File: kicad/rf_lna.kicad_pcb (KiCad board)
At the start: 4 copper layers, 100 x 100 mm, 69 parts, among them J1 Conn_01x02_Pin, J2 Conn_Coaxial_Small, J3 Conn_Coaxial_Small, J4 Conn_01x02_Pin, J5 Conn_Coaxial_Small, J6 Conn_Coaxial_Small, J7 Conn_Coaxial_Small, J8 Conn_Coaxial_Small, J9 Conn_Coaxial_Small, U1 L78L05_SOT89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

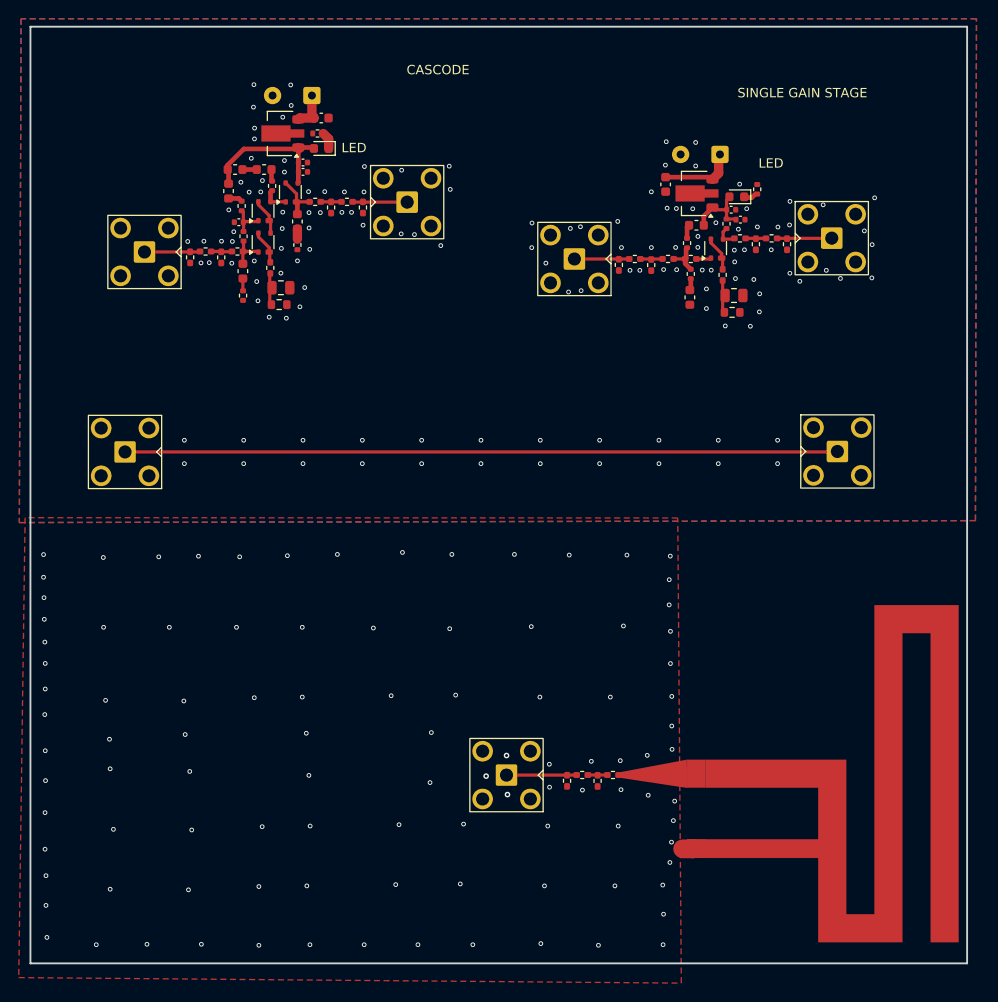
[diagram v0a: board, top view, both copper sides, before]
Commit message: files ready for production, but with wrong stackup (3313)
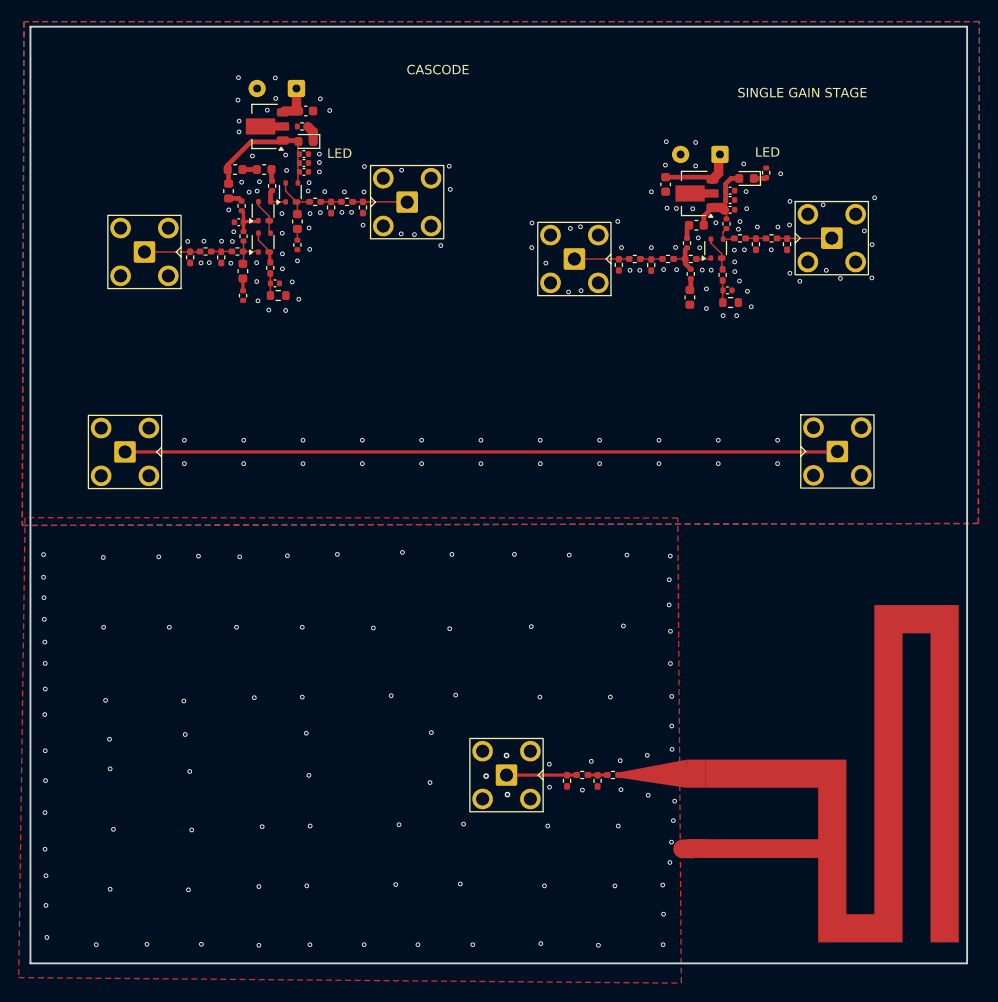
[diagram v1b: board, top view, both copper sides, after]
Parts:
- removed C18: 2.2nF, Capacitor_SMD:C_0805_2012Metric
- added C4: 100pF, Capacitor_SMD:C_0402_1005Metric, F.Cu at (79.2, 65.5)
- added C5: 100pF, Capacitor_SMD:C_0402_1005Metric, F.Cu at (124.7, 68.5)
- added C6: 100pF, Capacitor_SMD:C_0402_1005Metric, F.Cu at (124.4, 78.2)
- C7: value 2.2nF -> 100pF; footprint Capacitor_SMD:C_0805_2012Metric -> Capacitor_SMD:C_0402_1005Metric
- moved C7 49.0 mm to (76.1, 77.4)
- moved D1 2.22 mm to (126.5, 66.2)
- moved C2 2.04 mm to (124.7, 67.5)
- moved R1 2.00 mm to (128.6, 65.6)
- moved R2 1.81 mm to (79.0, 60.6)
- moved U5 1.81 mm to (75.0, 60.6)
- moved C11 1.81 mm to (79.4, 59.0)
- moved D2 1.81 mm to (79.4, 62.2)
- moved J4 1.81 mm to (78.4, 56.6)
- moved C3 1.52 mm to (124.7, 69.5)
- moved R4 1.06 mm to (124.8, 79.5)
- moved R15 0.98 mm to (76.5, 78.7)
- moved C14 0.96 mm to (79.2, 64.5)
- moved C12 0.91 mm to (79.2, 63.6)
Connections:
- R14 pad 2: Net-(C18-Pad1) -> Net-(C7-Pad1)
- R15 pad 1: Net-(C18-Pad1) -> Net-(C7-Pad1)
- R4 pad 1: Net-(C7-Pad1) -> Net-(C6-Pad1)
- R7 pad 1: Net-(C7-Pad1) -> Net-(C6-Pad1)
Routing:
- net +5C: track 7.35 -> 10.8 mm
- net Net-(C18-Pad1): track 3.37 -> 0.00 mm
- net Net-(C6-Pad1): track 0.00 -> 2.36 mm
- net Net-(C7-Pad1): track 3.48 -> 2.39 mm
- net +5V: track 16.0 -> 15.0 mm
- net +BATT: track 4.23 -> 3.70 mm
- net GND: vias 233 -> 242

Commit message: placed jlcpcb order, waiting for gerber confirmation
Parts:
- added FID1: Fiducial, Fiducial:Fiducial_1mm_Mask2mm, F.Cu at (141.9, 62.1)
- added FID2: Fiducial, Fiducial:Fiducial_1mm_Mask2mm, F.Cu at (57.1, 56.1)
- added FID3: Fiducial, Fiducial:Fiducial_1mm_Mask2mm, F.Cu at (123.8, 146.8)
- added H1: MountingHole, antennas:MountingHole_1.152mm_jlcpcb, F.Cu at (144.9, 100.9)
- added H2: MountingHole, antennas:MountingHole_1.152mm_jlcpcb, F.Cu at (110.9, 56.4)
- added H3: MountingHole, antennas:MountingHole_1.152mm_jlcpcb, F.Cu at (53.6, 146.8)
- added H4: MountingHole, antennas:MountingHole_1.152mm_jlcpcb, F.Cu at (54.2, 100.0)
